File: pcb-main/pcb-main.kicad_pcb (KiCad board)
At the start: 2 copper layers, 84 x 84 mm, 25 parts, among them J1 AVR-ISP-6, M1 Stepper_Motor, U1 ATmega328P-AU, U2 HT1621B, U3 VIM878

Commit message: added stepper motor spike (and heaps of other stuff)
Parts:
- removed D10, D12, D13, D9: LED, LED_SMD:LED_1206_3216Metric_Pad1.42x1.75mm_HandSolder
- removed R1, R2, R4, R5: R, Resistor_SMD:R_1206_3216Metric_Pad1.30x1.75mm_HandSolder
- added C1: C, Capacitor_SMD:C_1206_3216Metric_Pad1.33x1.80mm_HandSolder, F.Cu at (150.6, 60.0)
- added C2: C, Capacitor_SMD:C_1206_3216Metric_Pad1.33x1.80mm_HandSolder, F.Cu at (129.4, 66.5)
- added C3: C, Capacitor_SMD:C_1206_3216Metric_Pad1.33x1.80mm_HandSolder, F.Cu at (129.4, 71.5)
- added C4: C, Capacitor_SMD:C_1206_3216Metric_Pad1.33x1.80mm_HandSolder, F.Cu at (165.6, 127.0)
- added J2: Conn_02x06_Counter_Clockwise, Connector_PinHeader_2.54mm:PinHeader_2x06_P2.54mm_Vertical_SMD, B.Cu at (170.5, 75.3)
- added J3: Conn_02x02_Counter_Clockwise, Connector_PinHeader_2.54mm:PinHeader_2x02_P2.54mm_Vertical_SMD, F.Cu at (170.5, 70.3)
- added R7: 10k, Resistor_SMD:R_1206_3216Metric_Pad1.30x1.75mm_HandSolder, F.Cu at (118.0, 92.5)
- added Y1: Crystal, Crystal:Crystal_HC49-4H_Vertical, F.Cu at (135.0, 66.5)
- D1, D2, D3, D4, D5, D6, D7, D8: moved to B.Cu
- D11, D14: value LED -> BACKLIGHT
- J1: footprint Connector_PinSocket_2.54mm:PinSocket_2x03_P2.54mm_Vertical_SMD -> Connector_PinHeader_2.54mm:PinHeader_2x03_P2.54mm_Vertical
- U2: footprint Package_SO:SSOP-48_7.5x15.9mm_P0.635mm -> footprints:HT1621B
- moved D2 85.3 mm to (154.5, 91.0), turned to 180 degrees
- moved D3 78.1 mm to (154.5, 101.0)
- moved D4 72.6 mm to (154.5, 97.0), turned to 180 degrees
- moved D1 71.8 mm to (154.5, 87.0)
- moved D5 59.9 mm to (145.5, 87.0), turned to 180 degrees
- moved J1 52.2 mm to (114.0, 98.0)
- moved D6 51.5 mm to (145.5, 91.0)
- moved D7 45.0 mm to (145.5, 101.0), turned to 180 degrees
- moved D8 39.8 mm to (145.5, 97.0)
- moved U1 10.8 mm to (150.0, 68.2), turned to 270 degrees
- moved D11 2.02 mm to (136.0, 122.5)
- moved R3 1.76 mm to (131.0, 122.5)
- moved R6 0.76 mm to (169.0, 122.5)
- moved U3 0.58 mm to (124.0, 113.5)
- moved D14 0.41 mm to (164.2, 122.5)
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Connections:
- D1 pad 2: /MOT3 -> /MOT_3
- D11 pad 2: +5V -> /BACKLIGHT_LED
- D14 pad 2: +5V -> /BACKLIGHT_LED
- D2 pad 1: /MOT3 -> /MOT_3
- D3 pad 2: /MOT4 -> /MOT_4
- D4 pad 1: /MOT4 -> /MOT_4
- D5 pad 2: /MOT2 -> /MOT_2
- D6 pad 1: /MOT2 -> /MOT_2
- D7 pad 2: /MOT1 -> /MOT_1
- D8 pad 1: /MOT1 -> /MOT_1
- J1 pad 1: /MISO -> /PB4
- J1 pad 3: /SCK -> /PB5
- J1 pad 4: /MOSI -> /PB3
- M1 pad 1: /MOT1 -> /MOT_1
- M1 pad 2: /MOT2 -> /MOT_2
- M1 pad 3: /MOT3 -> /MOT_3
- M1 pad 4: /MOT4 -> /MOT_4
- U1 pad 1: Net-(U1-Pad1) -> /PD3
- U1 pad 10: Net-(U1-Pad10) -> /PD6
- U1 pad 11: Net-(U1-Pad11) -> /PD7
- U1 pad 12: Net-(U1-Pad12) -> /PB0
- U1 pad 15: /MOSI -> /PB3
- U1 pad 16: /MISO -> /PB4
- U1 pad 17: /SCK -> /PB5
- U1 pad 19: Net-(U1-Pad19) -> /ADC6
- U1 pad 2: Net-(U1-Pad2) -> /PD4
- U1 pad 20: Net-(U1-Pad20) -> +5V
- U1 pad 21: Net-(U1-Pad21) -> GND
- U1 pad 22: Net-(U1-Pad22) -> /ADC7
- U1 pad 23: /MOT1 -> /MOT_2
- U1 pad 24: /MOT2 -> /MOT_1
- U1 pad 25: /MOT3 -> /MOT_4
- U1 pad 26: /MOT4 -> /MOT_3
- U1 pad 27: Net-(U1-Pad27) -> /BACKLIGHT_LED
- U1 pad 3: Net-(U1-Pad21) -> GND
- U1 pad 30: Net-(U1-Pad30) -> /PD0
- U1 pad 31: Net-(U1-Pad31) -> /PD1
- U1 pad 32: Net-(U1-Pad32) -> /PD2
- U1 pad 5: Net-(U1-Pad21) -> GND
- U1 pad 7: Net-(U1-Pad7) -> /XTAL1
- U1 pad 8: Net-(U1-Pad8) -> /XTAL2
- U1 pad 9: Net-(U1-Pad9) -> /PD5
- U2 pad 11: /WR -> /PB4
- U2 pad 12: /DATA -> /PB5
- U2 pad 9: /CS -> /PB3
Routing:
- net +5V: track 0.00 -> 181.6 mm, vias 0 -> 4
- net /PB4: track 0.00 -> 92.1 mm, vias 0 -> 3
- net /PB5: track 0.00 -> 91.7 mm, vias 0 -> 3
- net /PB3: track 0.00 -> 89.9 mm, vias 0 -> 3
- net /BACKLIGHT_LED: track 0.00 -> 87.7 mm, vias 0 -> 2
- net /RESET: track 0.00 -> 63.9 mm, vias 0 -> 2
- net GND: track 0.00 -> 44.0 mm, vias 0 -> 10
- net /MOT_1: track 0.00 -> 41.0 mm
- net /MOT_4: track 0.00 -> 39.5 mm
- net /MOT_2: track 0.00 -> 36.7 mm
- net /MOT_3: track 0.00 -> 33.3 mm
- net /PD1: track 0.00 -> 28.6 mm, vias 0 -> 1
- net /PD2: track 0.00 -> 27.3 mm, vias 0 -> 1
- net /PB0: track 0.00 -> 25.9 mm, vias 0 -> 1
- net /PD7: track 0.00 -> 25.8 mm, vias 0 -> 1
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- added copper zone on B.Cu, net GND
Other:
- outline, holes or cut-outs redrawn
- board text added: "5V"
- board text added: "GND"
- board text added: "RST"

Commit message: cleaned up main pcb
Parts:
- added U4: TLSM, footprints:TLSM, F.Cu at (120.0, 111.0)
- moved D2 11.0 mm to (165.5, 90.0), turned to 0 degrees
- moved D4 11.0 mm to (165.5, 98.0), turned to 0 degrees
- moved D6 11.0 mm to (134.5, 90.0), turned to 180 degrees
- moved D8 11.0 mm to (134.5, 98.0), turned to 180 degrees
- moved D1 4.24 mm to (157.5, 90.0)
- moved D3 4.24 mm to (157.5, 98.0)
- moved D5 4.24 mm to (142.5, 90.0)
- moved D7 4.24 mm to (142.5, 98.0)
- moved J1 2.00 mm to (116.0, 98.0)
- moved R7 2.00 mm to (120.0, 92.5)
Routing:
- net GND: track 44.0 -> 55.3 mm
- net /MOT_2: track 36.7 -> 28.5 mm
- net +5V: track 181.6 -> 174.2 mm
- net /MOT_1: track 41.0 -> 36.4 mm
- net /MOT_4: track 39.5 -> 34.9 mm
- net /MOT_3: track 33.3 -> 28.7 mm
- net /RESET: track 63.9 -> 66.9 mm
- net /PB5: track 91.7 -> 90.1 mm
- net /PB4: track 92.1 -> 90.5 mm
- net /PB3: track 89.9 -> 88.3 mm
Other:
- outline, holes or cut-outs redrawn
- board text added: "ADC6"
- board text added: "ADC7"
- board text added: "MI"
- board text added: "MO"
- board text added: "PB0"
- board text added: "PD0"
- board text added: "PD1"
- board text added: "PD2"
- board text added: "PD3"
- board text added: "PD4"
- board text added: "PD5"
- board text added: "PD6"
- board text added: "PD7"
- board text added: "SCK"
- board text added: "Vcc"

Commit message: v1.0
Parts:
- U3: value VIM878 -> VIM-878-DP
- moved U4 2.24 mm to (119.0, 113.0)
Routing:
- net GND: track 55.3 -> 54.0 mm, vias 10 -> 9
- net /RESET: track 66.9 -> 67.4 mm
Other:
- outline, holes or cut-outs redrawn
- board text added: "JLCJLCJLCJLC"
- board text added: "MISO"
- board text added: "MOSI"
- board text added: "Motorcycle Tacho v1.0"
- board text added: "VCC"
- board text removed: "MI"
- board text removed: "MO"
- board text removed: "Vcc"

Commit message: add oshw logo
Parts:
- added G***: LOGO, footprints:OSHW, F.Cu at (180.5, 120.5)

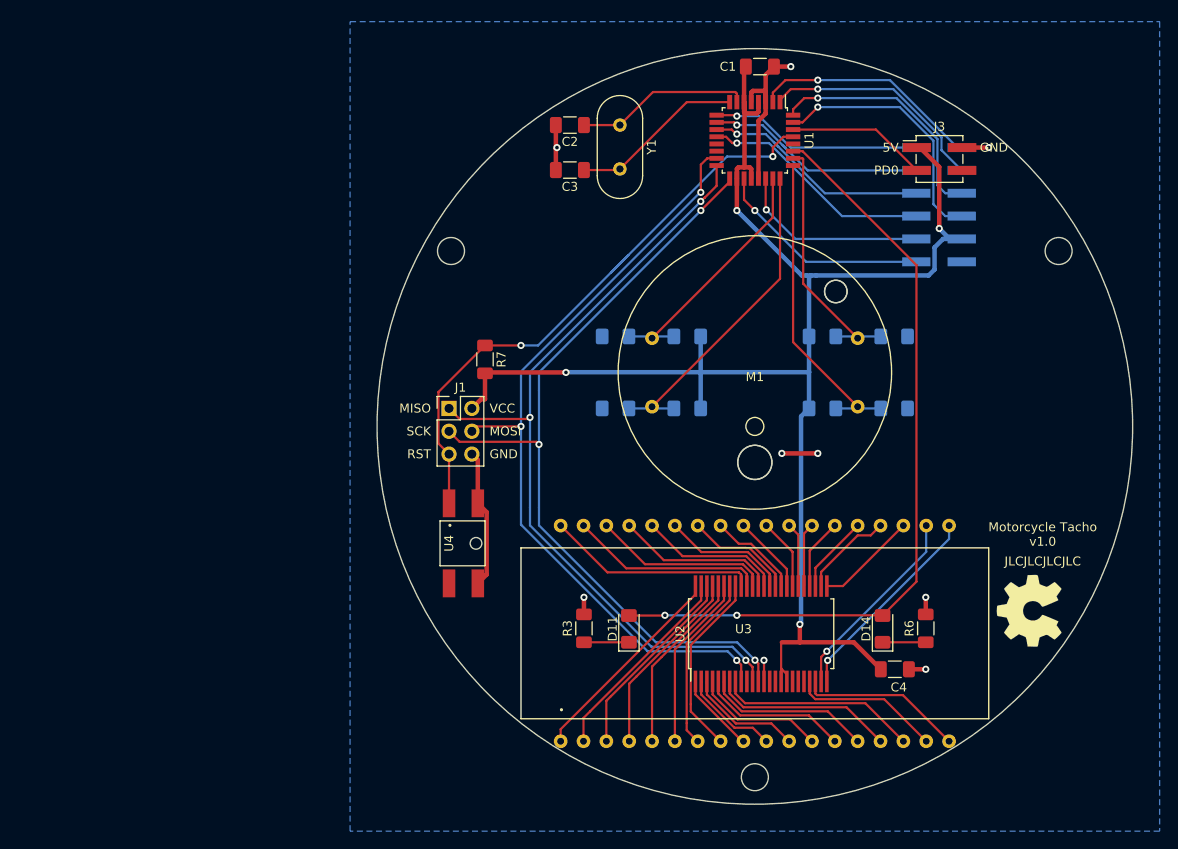
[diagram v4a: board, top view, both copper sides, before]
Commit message: made pcb bigger
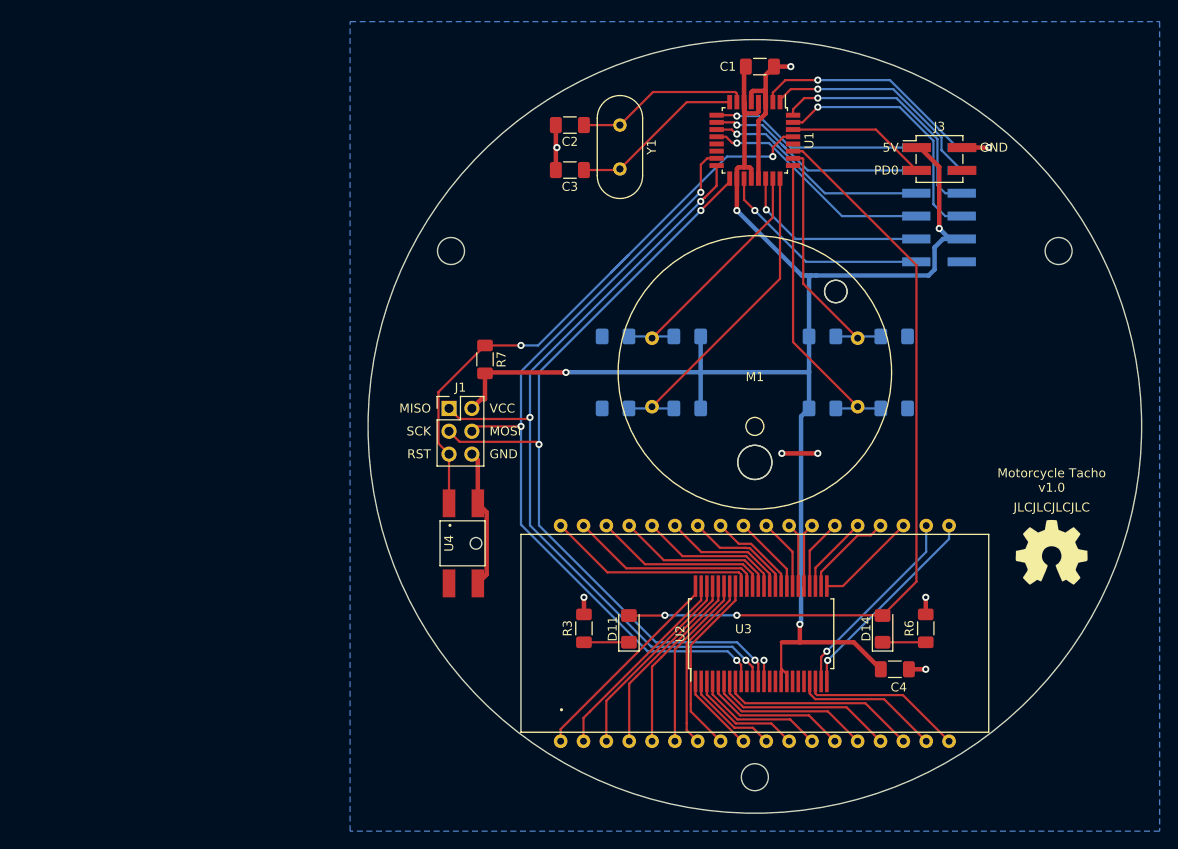
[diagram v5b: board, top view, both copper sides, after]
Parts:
- moved G*** 6.96 mm to (183.0, 114.0), turned to 0 degrees
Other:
- board size 84 x 84 mm -> 86 x 86 mm

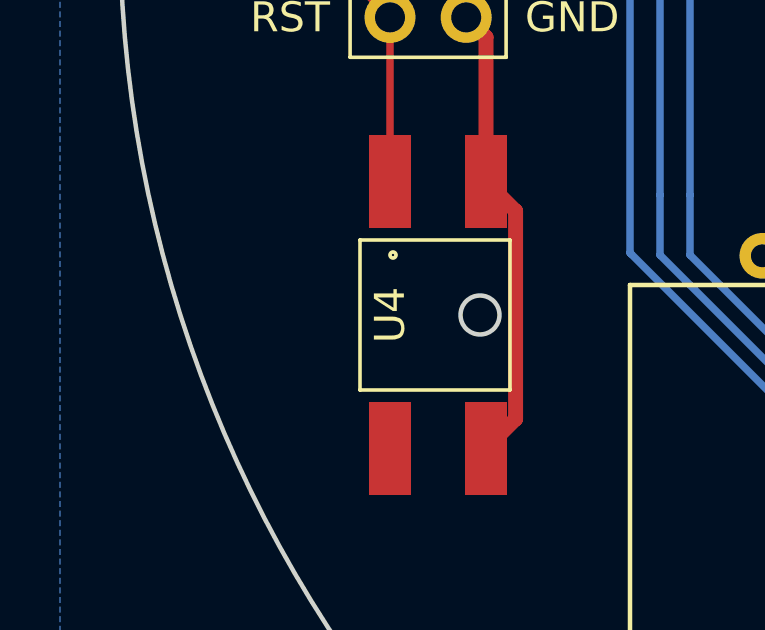
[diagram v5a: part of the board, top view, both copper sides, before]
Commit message: reset button label
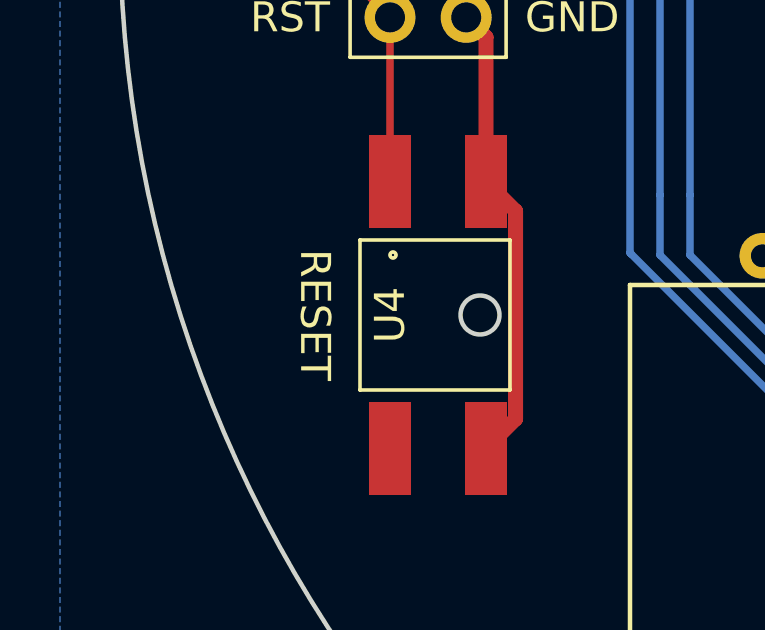
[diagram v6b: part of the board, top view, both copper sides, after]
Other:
- board text added: "RESET"

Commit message: started v1.1
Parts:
- removed G***: LOGO, footprints:OSHW
- removed J3: Conn_02x02_Counter_Clockwise, Connector_PinHeader_2.54mm:PinHeader_2x02_P2.54mm_Vertical_SMD
- removed R6: R, Resistor_SMD:R_1206_3216Metric_Pad1.30x1.75mm_HandSolder
- added BT1: Battery_Cell, footprints:CR1220, B.Cu at (177.5, 99.5)
- added C5: 100n, Capacitor_SMD:C_1206_3216Metric_Pad1.33x1.80mm_HandSolder, F.Cu at (184.4, 109.0)
- added D10: WS2812B, LED_SMD:LED_WS2812B_PLCC4_5.0x5.0mm_P3.2mm, F.Cu at (130.0, 105.0)
- added D12: WS2812B, LED_SMD:LED_WS2812B_PLCC4_5.0x5.0mm_P3.2mm, F.Cu at (166.6, 123.1)
- added D13: WS2812B, LED_SMD:LED_WS2812B_PLCC4_5.0x5.0mm_P3.2mm, F.Cu at (170.0, 105.0)
- added D15: D, Diode_SMD:D_1206_3216Metric_Pad1.42x1.75mm_HandSolder, F.Cu at (184.5, 105.5)
- added D16: D, Diode_SMD:D_1206_3216Metric_Pad1.42x1.75mm_HandSolder, F.Cu at (184.5, 102.5)
- added D9: WS2812B, LED_SMD:LED_WS2812B_PLCC4_5.0x5.0mm_P3.2mm, F.Cu at (130.0, 95.0)
- added R1: 10k, Resistor_SMD:R_1206_3216Metric_Pad1.30x1.75mm_HandSolder, F.Cu at (165.6, 117.5)
- added R2: R, Resistor_SMD:R_1206_3216Metric_Pad1.30x1.75mm_HandSolder, F.Cu at (184.4, 90.0)
- added SW1: SW_MEC_5E, footprints:TS_1187A, F.Cu at (178.5, 76.5)
- added Y2: Crystal, Crystal:Crystal_SMD_EuroQuartz_EQ161-2Pin_3.2x1.5mm_HandSoldering, F.Cu at (190.0, 96.1)
- C1: value C -> 0.1u
- C2, C3: value C -> 22p
- D11, D14: value BACKLIGHT -> WS2812B; footprint LED_SMD:LED_1206_3216Metric_Pad1.42x1.75mm_HandSolder -> LED_SMD:LED_WS2812B_PLCC4_5.0x5.0mm_P3.2mm
- J2: footprint Connector_PinHeader_2.54mm:PinHeader_2x06_P2.54mm_Vertical_SMD -> Connector_PinSocket_2.54mm:PinSocket_2x06_P2.54mm_Vertical; moved to F.Cu
- R3: value R -> 10k
- U3: value VIM-878-DP -> VIM878
- U4: value TLSM -> PCF8563T; footprint footprints:TLSM -> Package_SO:SOIC-8_3.9x4.9mm_P1.27mm
- Y1: value Crystal -> 16MHz
- moved U4 67.3 mm to (184.1, 96.0)
- moved R3 61.1 mm to (178.4, 84.0), turned to 180 degrees
- moved D14 28.1 mm to (170.0, 95.0), turned to 0 degrees
- moved D2 8.36 mm to (157.5, 92.5), turned to 180 degrees
- moved D4 8.36 mm to (157.5, 95.5), turned to 180 degrees
- moved D6 8.36 mm to (142.5, 92.5), turned to 0 degrees
- moved D8 8.36 mm to (142.5, 95.5), turned to 0 degrees
- moved J2 6.52 mm to (169.0, 69.0), turned to 0 degrees
- moved C2 6.45 mm to (134.7, 62.8)
- moved C3 6.45 mm to (134.7, 67.8)
- moved Y1 6.45 mm to (140.2, 62.8)
- moved R7 3.67 mm to (116.5, 93.5), turned to 0 degrees
- moved D11 2.62 mm to (133.4, 123.1), turned to 0 degrees
- moved C4 1.00 mm to (165.6, 128.0)
- moved J1 0.54 mm to (115.5, 98.0)
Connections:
- net Net-(U1-Pad13) renamed /PB1
- D11 pad 1: Net-(D11-Pad1) -> +5V
- D11 pad 2: /BACKLIGHT_LED -> Net-(D11-Pad2)
- D14 pad 1: Net-(D14-Pad1) -> +5V
- D14 pad 2: /BACKLIGHT_LED -> Net-(D14-Pad2)
- R3 pad 1: Net-(D11-Pad1) -> /PD1
- R3 pad 2: GND -> +5V
- U1 pad 14: Net-(U1-Pad14) -> /PB2
- U1 pad 27: /BACKLIGHT_LED -> /PC4
- U1 pad 28: Net-(U1-Pad28) -> /PC5
- U2 pad 16: +5V -> Net-(R1-Pad2)
- U4 pad 1: /RESET -> Net-(U4-Pad1)
- U4 pad 3: GND -> Net-(R2-Pad1)
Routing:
- net /BACKLIGHT_LED: track 87.7 -> 0.00 mm, vias 2 -> 0
- net Net-(D11-Pad2): track 0.00 -> 73.7 mm
- net +5V: track 174.2 -> 244.0 mm, vias 4 -> 5
- net /PC5: track 0.00 -> 44.9 mm
- net /PC4: track 0.00 -> 43.7 mm
- net GND: track 54.0 -> 95.6 mm, vias 9 -> 10
- net /PB2: track 0.00 -> 30.0 mm
- net Net-(D12-Pad2): track 0.00 -> 24.8 mm
- net Net-(D10-Pad2): track 0.00 -> 18.8 mm
- net Net-(BT1-Pad1): track 0.00 -> 16.9 mm, vias 0 -> 1
- net Net-(R1-Pad2): track 0.00 -> 16.4 mm
- net /PD0: track 15.6 -> 0.00 mm
- net Net-(D13-Pad2): track 0.00 -> 15.2 mm
- net /PD1: track 28.6 -> 43.1 mm, vias 1 -> 0
- net /PD2: track 27.3 -> 18.3 mm, vias 1 -> 0
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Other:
- outline, holes or cut-outs redrawn
- board text added: "MODE"
- board text added: "Motorcycle Tacho v1.1"
- board text removed: "Motorcycle Tacho v1.0"
- board text removed: "PD0"
- board text removed: "RESET"

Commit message: v1.1
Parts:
- C1: value 0.1u -> 100n
- C4: value C -> 100n
- D15, D16: value D -> 1N4001
- R2: value R -> 10k
- U2: value HT1621B -> HT1621B-LQFP-A; footprint footprints:HT1621B -> Package_QFP:LQFP-48_7x7mm_P0.5mm
- Y2: footprint Crystal:Crystal_SMD_EuroQuartz_EQ161-2Pin_3.2x1.5mm_HandSoldering -> Crystal:Crystal_C26-LF_D2.1mm_L6.5mm_Horizontal
- moved C4 26.4 mm to (139.5, 123.6), turned to 270 degrees
- moved R1 24.3 mm to (142.0, 123.5), turned to 90 degrees
- moved Y2 4.39 mm to (188.5, 92.0), turned to 0 degrees
- turned U2 to 0 degrees
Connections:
- C5 pad 1: +5V -> Net-(C5-Pad1)
- D15 pad 1: Net-(D15-Pad1) -> Net-(C5-Pad1)
- D16 pad 1: Net-(D15-Pad1) -> Net-(C5-Pad1)
- U2 pad 1: /SEG7 -> /PB5
- U2 pad 11: /PB4 -> Net-(U2-Pad11)
- U2 pad 12: /PB5 -> Net-(U2-Pad12)
- U2 pad 13: GND -> /COM0
- U2 pad 14: Net-(U2-Pad14) -> /COM1
- U2 pad 15: Net-(U2-Pad15) -> /COM2
- U2 pad 16: Net-(R1-Pad2) -> /COM3
- U2 pad 17: +5V -> /SEG31
- U2 pad 18: Net-(U2-Pad18) -> /SEG30
- U2 pad 19: Net-(U2-Pad19) -> /SEG29
- U2 pad 2: /SEG6 -> Net-(U2-Pad2)
- U2 pad 20: Net-(U2-Pad20) -> /SEG27
- U2 pad 21: /COM0 -> /SEG28
- U2 pad 22: /COM1 -> /SEG26
- U2 pad 23: /COM2 -> /SEG25
- U2 pad 24: /COM3 -> /SEG24
- U2 pad 25: /SEG31 -> /SEG23
- U2 pad 26: /SEG30 -> /SEG22
- U2 pad 27: /SEG29 -> /SEG21
- U2 pad 28: /SEG28 -> /SEG20
- U2 pad 29: /SEG27 -> /SEG19
- U2 pad 3: /SEG5 -> /PB4
- U2 pad 30: /SEG26 -> /SEG18
- U2 pad 31: /SEG25 -> /SEG17
- U2 pad 32: /SEG24 -> /SEG16
- U2 pad 33: /SEG23 -> /SEG15
- U2 pad 34: /SEG22 -> /SEG14
- U2 pad 35: /SEG21 -> /SEG13
- U2 pad 36: /SEG20 -> /SEG12
- U2 pad 37: /SEG19 -> /SEG11
- U2 pad 38: /SEG18 -> /SEG10
- U2 pad 39: /SEG17 -> /SEG9
- U2 pad 4: /SEG4 -> /PB3
- U2 pad 40: /SEG16 -> /SEG8
- U2 pad 41: /SEG15 -> /SEG7
- U2 pad 42: /SEG14 -> /SEG6
- U2 pad 43: /SEG13 -> /SEG5
- U2 pad 44: /SEG12 -> /SEG4
- U2 pad 45: /SEG11 -> /SEG3
- U2 pad 46: /SEG10 -> /SEG2
- U2 pad 47: /SEG9 -> /SEG1
- U2 pad 48: /SEG8 -> /SEG0
- U2 pad 5: /SEG3 -> GND
- U2 pad 6: /SEG2 -> Net-(U2-Pad6)
- U2 pad 7: /SEG1 -> Net-(U2-Pad7)
- U2 pad 8: /SEG0 -> Net-(R1-Pad2)
- U2 pad 9: /PB3 -> +5V
- U3 pad 1: /SEG8 -> /SEG31
- U3 pad 10: /SEG6 -> /SEG22
- U3 pad 11: /SEG5 -> /SEG21
- U3 pad 12: /SEG4 -> /SEG20
- U3 pad 13: /SEG3 -> /SEG19
- U3 pad 14: /SEG2 -> /SEG18
- U3 pad 15: /SEG1 -> /SEG17
- U3 pad 16: /SEG0 -> /SEG16
- U3 pad 19: /COM3 -> /COM2
- U3 pad 2: /SEG9 -> /SEG30
- U3 pad 20: /COM2 -> /COM3
- U3 pad 21: /SEG31 -> /SEG15
- U3 pad 22: /SEG30 -> /SEG14
- U3 pad 23: /SEG29 -> /SEG13
- U3 pad 24: /SEG28 -> /SEG12
- U3 pad 25: /SEG27 -> /SEG11
- U3 pad 26: /SEG26 -> /SEG10
- U3 pad 27: /SEG25 -> /SEG9
- U3 pad 28: /SEG24 -> /SEG8
- U3 pad 29: /SEG23 -> /SEG7
- U3 pad 3: /SEG10 -> /SEG29
- U3 pad 30: /SEG22 -> /SEG6
- U3 pad 31: /SEG21 -> /SEG5
- U3 pad 32: /SEG20 -> /SEG4
- U3 pad 33: /SEG19 -> /SEG3
- U3 pad 34: /SEG18 -> /SEG2
- U3 pad 35: /SEG17 -> /SEG1
- U3 pad 36: /SEG16 -> /SEG0
- U3 pad 4: /SEG11 -> /SEG27
- U3 pad 5: /SEG12 -> /SEG28
- U3 pad 6: /SEG13 -> /SEG26
- U3 pad 7: /SEG14 -> /SEG25
- U3 pad 8: /SEG15 -> /SEG24
- U3 pad 9: /SEG7 -> /SEG23
- U4 pad 8: Net-(D15-Pad1) -> Net-(C5-Pad1)
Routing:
- net /SEG31: track 11.3 -> 26.7 mm
- net /SEG8: track 23.5 -> 9.19 mm
- net /SEG9: track 22.3 -> 8.35 mm
- net /SEG10: track 21.5 -> 8.22 mm
- net /SEG29: track 8.67 -> 21.3 mm
- net /SEG27: track 7.09 -> 19.4 mm
- net /SEG30: track 11.0 -> 23.3 mm
- net Net-(C5-Pad1): track 0.00 -> 11.8 mm
- net /SEG11: track 20.7 -> 9.48 mm
- net Net-(R1-Pad2): track 16.4 -> 5.28 mm
- net /COM1: track 19.3 -> 29.9 mm, vias 0 -> 1
- net /SEG28: track 7.88 -> 17.4 mm
- net /COM0: track 17.4 -> 26.7 mm, vias 0 -> 1
- net /COM2: track 21.6 -> 30.9 mm
- net /SEG12: track 20.0 -> 10.9 mm
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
